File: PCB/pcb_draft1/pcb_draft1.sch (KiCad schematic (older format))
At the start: 79 parts, among them J1 RollerServos, J2 12V_Power A97996-ND, J3 HomeSwitch, J4 Therm1, J5 ArdAnalogTherm, J6 Therm2, J7 RasPi, Q1 DMN6140L, Q10 DMN6140L, Q11 DMN6140L, Q12 DMN6140L, Q13 DMN6140L, Q14 DMN6140L, Q15 DMN6140L, Q2 DMN6140L, Q3 DMN6140L, Q4 DMN6140L, Q5 DMN6140L, Q6 DMN6140L, Q7 DMN6140L, Q8 DMN6140L, Q9 DMN6140L, U1 STSPIN820, U2 STSPIN820, U3 AMS1117-5.0 RasPi, U4 AMS1117-5.0 Servo, Y1 Arduino_Mega_Bottom_Pins1

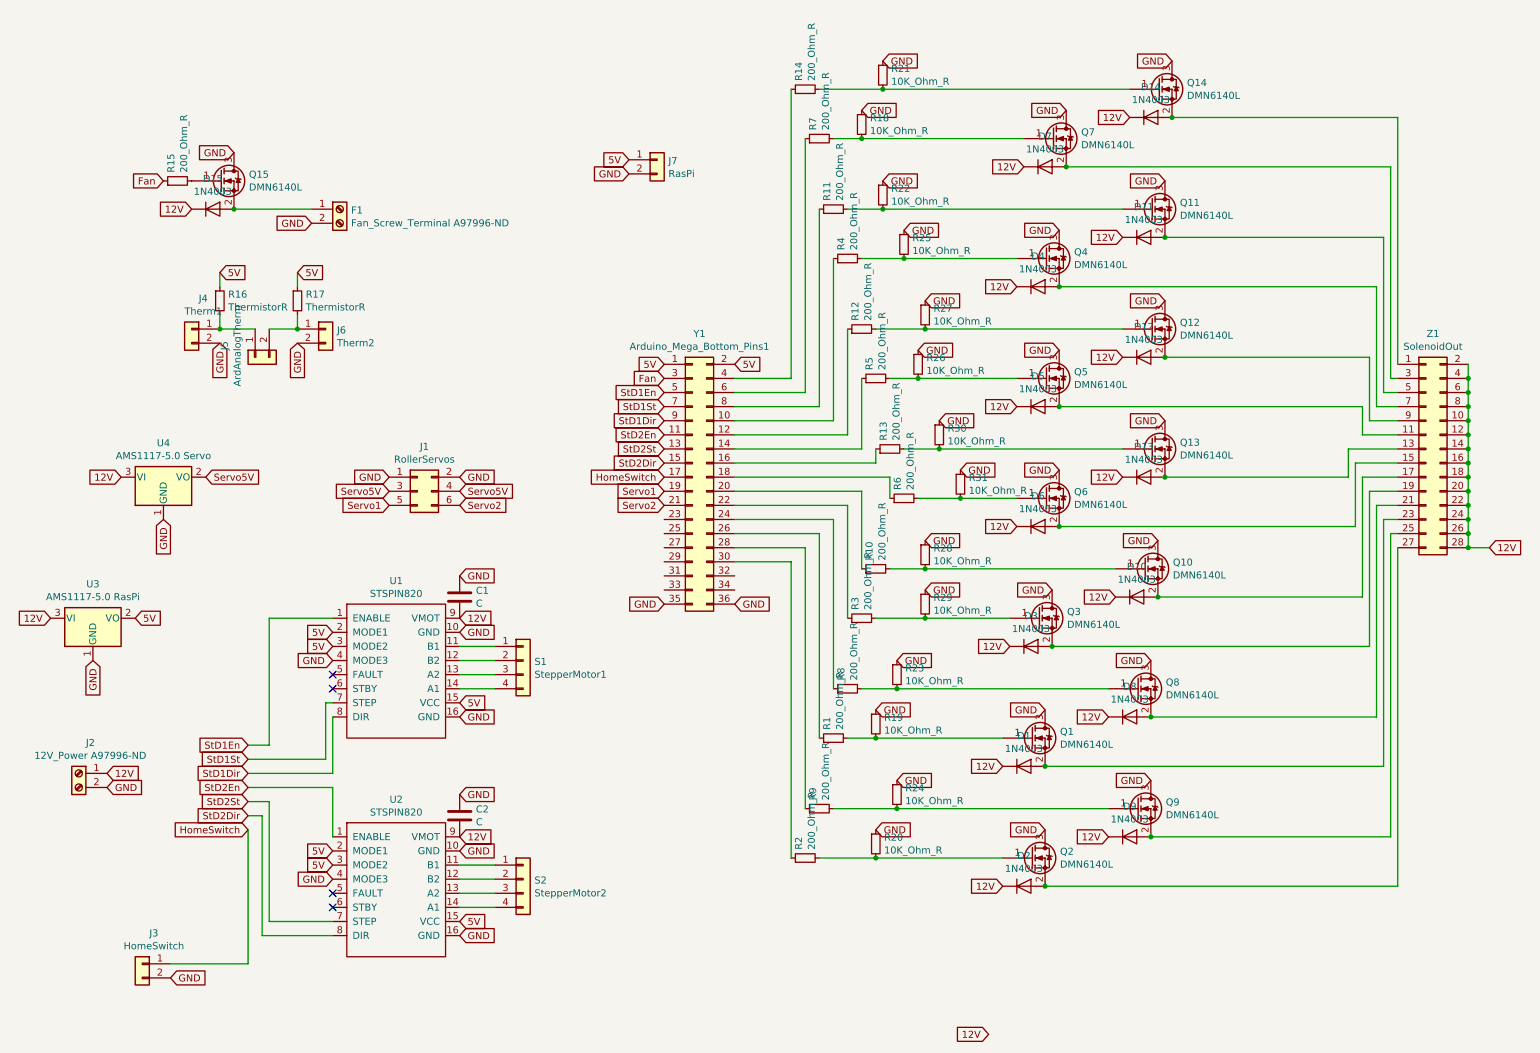
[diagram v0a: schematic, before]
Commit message: Run traces for preliminarily finished board
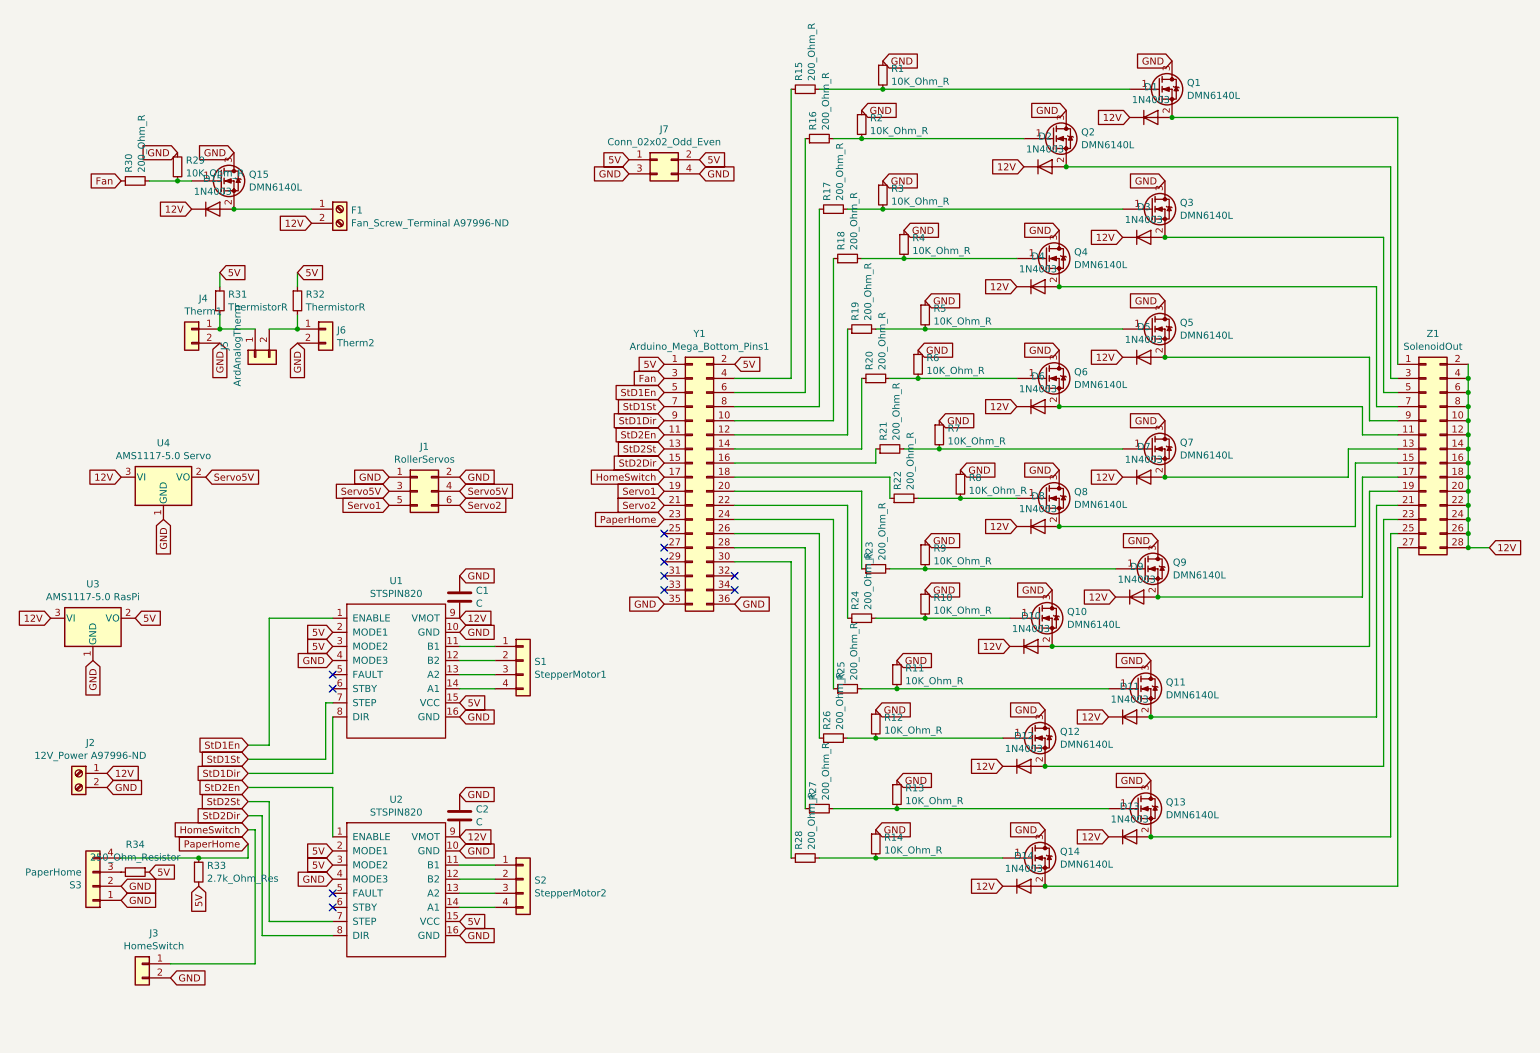
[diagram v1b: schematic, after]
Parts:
- removed J7: RasPi, Connector_PinHeader_2.54mm:PinHeader_1x02_P2.54mm_Vertical, symbol Connector_Generic:Conn_01x02
- added J7: Conn_02x02_Odd_Even, Connector_PinHeader_2.54mm:PinHeader_2x02_P2.54mm_Vertical, symbol Connector_Generic:Conn_02x02_Odd_Even
- added R29: 10K_Ohm_R, Resistor_SMD:R_0402_1005Metric, symbol Device:R_Small
- added R33: 2.7k_Ohm_Res, Resistor_SMD:R_0402_1005Metric, symbol Device:R_Small
- added R34: 250_Ohm_Resistor, Resistor_SMD:R_0603_1608Metric, symbol Device:R_Small
- added S3: PaperHome, Connector_PinHeader_2.54mm:PinHeader_1x04_P2.54mm_Vertical, symbol Connector_Generic:Conn_01x04
- R1: renamed from R21; footprint (none) -> Resistor_SMD:R_0402_1005Metric
- R10: renamed from R29; footprint (none) -> Resistor_SMD:R_0402_1005Metric
- R11: renamed from R23; footprint (none) -> Resistor_SMD:R_0402_1005Metric
- R12: renamed from R19; footprint (none) -> Resistor_SMD:R_0402_1005Metric
- R13: renamed from R24; footprint (none) -> Resistor_SMD:R_0402_1005Metric
- R14: renamed from R20; footprint (none) -> Resistor_SMD:R_0402_1005Metric
- R2: renamed from R18; footprint (none) -> Resistor_SMD:R_0402_1005Metric
- R3: renamed from R22; footprint (none) -> Resistor_SMD:R_0402_1005Metric
- R4: renamed from R25; footprint (none) -> Resistor_SMD:R_0402_1005Metric
- R5: renamed from R27; footprint (none) -> Resistor_SMD:R_0402_1005Metric
- R6: renamed from R26; footprint (none) -> Resistor_SMD:R_0402_1005Metric
- R7: renamed from R30; footprint (none) -> Resistor_SMD:R_0402_1005Metric
- R8: renamed from R31; footprint (none) -> Resistor_SMD:R_0402_1005Metric
- R9: renamed from R28; footprint (none) -> Resistor_SMD:R_0402_1005Metric
- renumbered D14 to D1, D3 to D10, D8 to D11, D1 to D12, D9 to D13, D2 to D14, D7 to D2, D11 to D3, D12 to D5, D5 to D6, D13 to D7, D6 to D8, D10 to D9, Q14 to Q1, Q3 to Q10, Q8 to Q11, Q1 to Q12, Q9 to Q13, Q2 to Q14, Q7 to Q2, Q11 to Q3, Q12 to Q5, Q5 to Q6, Q13 to Q7, Q6 to Q8, Q10 to Q9, R14 to R15, R7 to R16, R11 to R17, R4 to R18, R12 to R19, R5 to R20, R13 to R21, R6 to R22, R10 to R23, R3 to R24, R8 to R25, R1 to R26, R9 to R27, R2 to R28, R15 to R30, R16 to R31, R17 to R32
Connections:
- net 12V: now also F1.2 (Pin_2)
- net 5V: now also J7.1 (Pin_1), J7.2 (Pin_2), R33.2, R34.1
- net GND: now also J7.3 (Pin_3), J7.4 (Pin_4), R29.1, S3.1 (Pin_1), S3.2 (Pin_2); no longer F1.2 (Pin_2)
- net at Q15.1 (G), R30.2: now also R29.2
- net PaperHome: now reaches Y1.23 (Pin_23)
- net PaperHome: now also R33.1, S3.4 (Pin_4)
- new net: R34.2, S3.3 (Pin_3)
- no-connect marks 4 -> 11
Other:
- moved on the sheet: R30
